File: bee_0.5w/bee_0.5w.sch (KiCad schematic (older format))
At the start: 4 parts, among them J1 Conn_01x02_Male, J2 Conn_01x02_Male, J3 Conn_01x02_Male, J4 Conn_01x02_Male

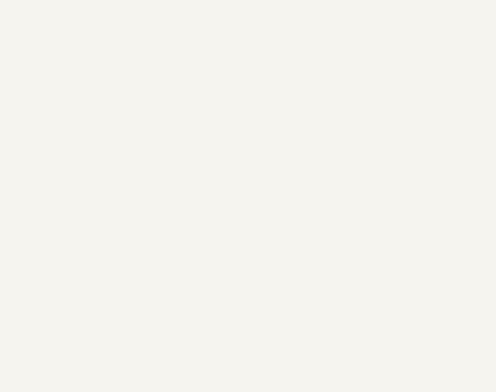
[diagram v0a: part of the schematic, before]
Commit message: Add sch symbols for labels, update PCB accordingly.
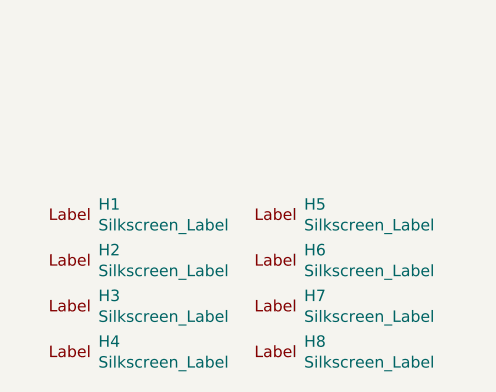
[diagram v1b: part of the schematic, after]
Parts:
- added H1, H2: Silkscreen_Label, Symbol-emt:Text_U_B+_Silkscreen, symbol Mechanical-emt:Silkscreen_Label
- added H3, H4: Silkscreen_Label, Symbol-emt:Text_U_B-_Silkscreen, symbol Mechanical-emt:Silkscreen_Label
- added H5, H6: Silkscreen_Label, Symbol-emt:Text_U_B2_Silkscreen, symbol Mechanical-emt:Silkscreen_Label
- added H7, H8: Silkscreen_Label, Symbol-emt:Symbol_GND_Silkscreen, symbol Mechanical-emt:Silkscreen_Label
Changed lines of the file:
@@
 EESchema Schematic File Version 4
-EELAYER 26 0
+LIBS:bee_0.5w-cache
+EELAYER 29 0
 EELAYER END
 $Descr A4 11693 8268
@@
 Wire Wire Line
 	1050 1400 1450 1400
+$Comp
+L Mechanical-emt:Silkscreen_Label H4
+U 1 1 5CC7157C
+P 800 7550
+F 0 "H4" H 925 7595 50  0000 L CNN
+F 1 "Silkscreen_Label" H 925 7504 50  0000 L CNN
+F 2 "Symbol-emt:Text_U_B-_Silkscreen" H 800 7550 50  0001 C CNN
+F 3 "~" H 800 7550 50  0001 C CNN
+	1    800  7550
+	1    0    0    -1
+$EndComp
+$Comp
+L Mechanical-emt:Silkscreen_Label H3
+U 1 1 5CC71DFD
+P 800 7350
+F 0 "H3" H 925 7395 50  0000 L CNN
+F 1 "Silkscreen_Label" H 925 7304 50  0000 L CNN
+F 2 "Symbol-emt:Text_U_B-_Silkscreen" H 800 7350 50  0001 C CNN
+F 3 "~" H 800 7350 50  0001 C CNN
+	1    800  7350
+	1    0    0    -1
+$EndComp
+$Comp
+L Mechanical-emt:Silkscreen_Label H2
+U 1 1 5CC72351
+P 800 7150
+F 0 "H2" H 925 7195 50  0000 L CNN
+F 1 "Silkscreen_Label" H 925 7104 50  0000 L CNN
+F 2 "Symbol-emt:Text_U_B+_Silkscreen" H 800 7150 50  0001 C CNN
+F 3 "~" H 800 7150 50  0001 C CNN
+	1    800  7150
+	1    0    0    -1
+$EndComp
+$Comp
+L Mechanical-emt:Silkscreen_Label H1
+U 1 1 5CC7235B
+P 800 6950
+F 0 "H1" H 925 6995 50  0000 L CNN
+F 1 "Silkscreen_Label" H 925 6904 50  0000 L CNN
+F 2 "Symbol-emt:Text_U_B+_Silkscreen" H 800 6950 50  0001 C CNN
+F 3 "~" H 800 6950 50  0001 C CNN
+	1    800  6950
+	1    0    0    -1
+$EndComp
+$Comp
+L Mechanical-emt:Silkscreen_Label H8
+U 1 1 5CC72A95
+P 1700 7550
+F 0 "H8" H 1825 7595 50  0000 L CNN
+F 1 "Silkscreen_Label" H 1825 7504 50  0000 L CNN
+F 2 "Symbol-emt:Symbol_GND_Silkscreen" H 1700 7550 50  0001 C CNN
+F 3 "~" H 1700 7550 50  0001 C CNN
+	1    1700 7550
+	1    0    0    -1
+$EndComp
+$Comp
+L Mechanical-emt:Silkscreen_Label H7
+U 1 1 5CC72A9F
+P 1700 7350
+F 0 "H7" H 1825 7395 50  0000 L CNN
+F 1 "Silkscreen_Label" H 1825 7304 50  0000 L CNN
+F 2 "Symbol-emt:Symbol_GND_Silkscreen" H 1700 7350 50  0001 C CNN
+F 3 "~" H 1700 7350 50  0001 C CNN
+	1    1700 7350
+	1    0    0    -1
+$EndComp
+$Comp
+L Mechanical-emt:Silkscreen_Label H6
+U 1 1 5CC72AA9
+P 1700 7150
+F 0 "H6" H 1825 7195 50  0000 L CNN
+F 1 "Silkscreen_Label" H 1825 7104 50  0000 L CNN
+F 2 "Symbol-emt:Text_U_B2_Silkscreen" H 1700 7150 50  0001 C CNN
+F 3 "~" H 1700 7150 50  0001 C CNN
+	1    1700 7150
+	1    0    0    -1
+$EndComp
+$Comp
+L Mechanical-emt:Silkscreen_Label H5
+U 1 1 5CC72AB3
+P 1700 6950
+F 0 "H5" H 1825 6995 50  0000 L CNN
+F 1 "Silkscreen_Label" H 1825 6904 50  0000 L CNN
+F 2 "Symbol-emt:Text_U_B2_Silkscreen" H 1700 6950 50  0001 C CNN
+F 3 "~" H 1700 6950 50  0001 C CNN
+	1    1700 6950
+	1    0    0    -1
+$EndComp
 $EndSCHEMATC
